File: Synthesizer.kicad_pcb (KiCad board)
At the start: 6 copper layers, 135.2 x 94.2 mm, 156 parts, among them J1 USB_A, J2 AudioJack3, J3 USB_B_Micro, J4 FPGA_debug, J5 MCU_debug, J6 MCU_GPIO, J7 FPGA_GPIO, SW1 SW_Push, SW10 SW_Push, SW11 SW_Push, SW12 SW_Push, SW13 SW_Push, SW14 SW_Push, SW15 SW_Push, SW16 SW_Push, SW2 SW_Push, SW3 SW_Push, SW4 SW_Push, SW5 SW_Push, SW6 SW_Push, SW7 SW_Push, SW8 SW_Push, SW9 SW_Push, U1 TPD3S014, U2 S25FL127S, U3 XC7A100T-FTG256, U4 Oscillator, U5 TPS54325, U6 TPS54294, U7 EFM32GG11B4xx, U8 PCM5102, Y1 48Mhz

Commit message: Fix one erroneous trace. VERY REVOLUTIONARY CHANGES
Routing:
- net +3V3: track 632.8 -> 632.2 mm
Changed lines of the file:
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@@
     (thickness 1.6)
     (drawings 4)
-    (tracks 1936)
+    (tracks 1935)
     (zones 0)
     (modules 156)
@@
   (segment (start 103.112 83.0343) (end 103.112 84.1636) (width 0.3) (layer F.Cu) (net 4))
   (segment (start 103.112 84.1636) (end 103.124 84.1756) (width 0.3) (layer F.Cu) (net 4))
-  (segment (start 107.3586 85.344) (end 108.0336 85.344) (width 0.3) (layer B.Cu) (net 4))
   (via (at 97.8662 87.9348) (size 0.48) (drill 0.25) (layers F.Cu B.Cu) (net 4))
   (segment (start 96.6995 87.9468) (end 97.8542 87.9468) (width 0.3) (layer F.Cu) (net 4))

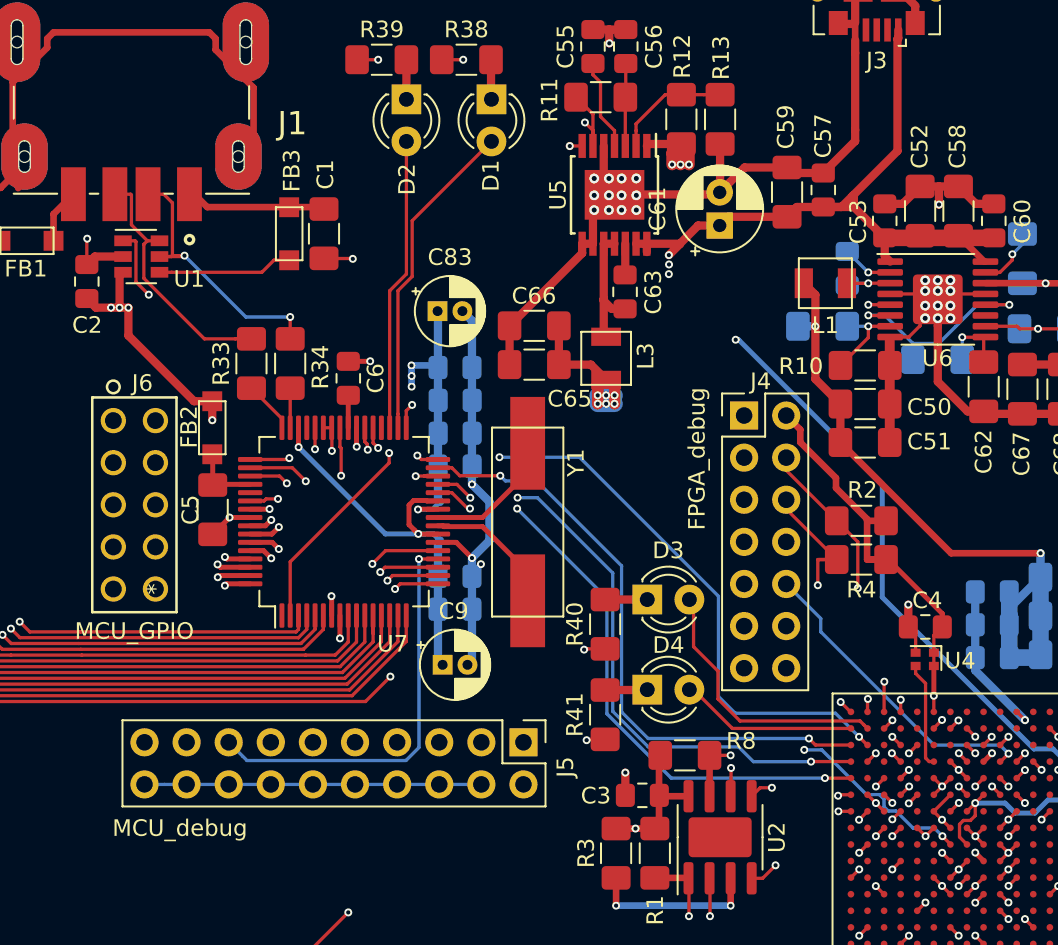
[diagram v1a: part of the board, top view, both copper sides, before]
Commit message: Changed a capacitor value from 100u to 150u. (oopsiedaisy)
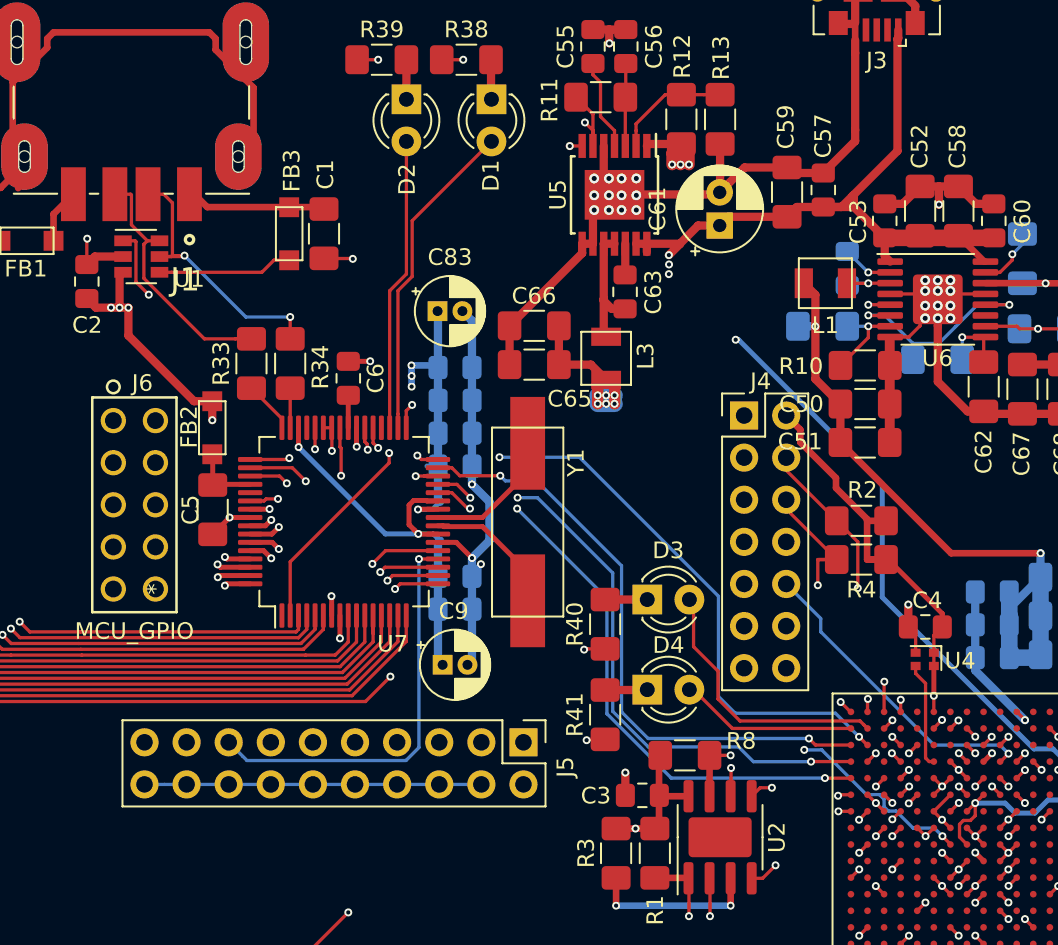
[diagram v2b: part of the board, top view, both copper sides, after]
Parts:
- removed the G*** at (171.3, 132.0)
- C1: value 100u -> 150u
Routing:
- net +3V3: track 632.2 -> 632.8 mm

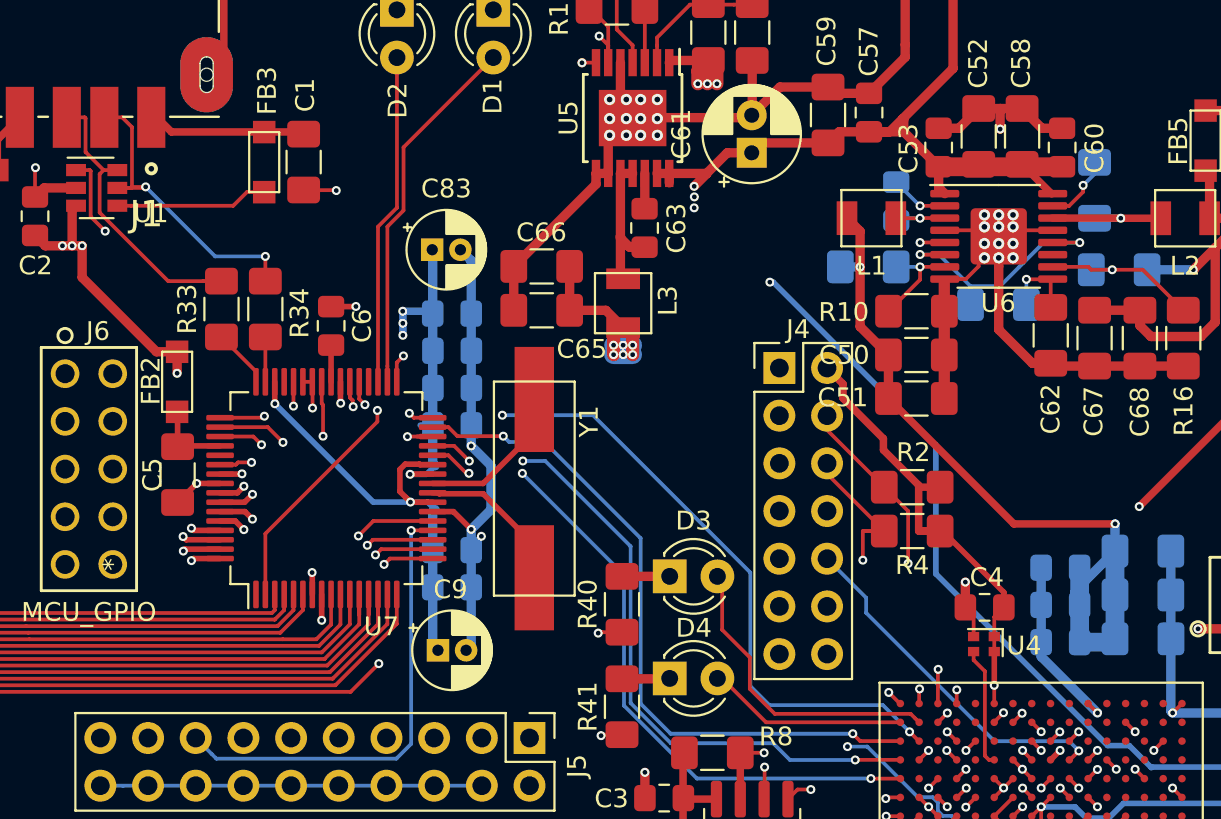
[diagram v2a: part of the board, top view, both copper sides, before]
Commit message: Replaced oscillator with a larger footprint and rewired. Also changed track width on some USB-A wires.
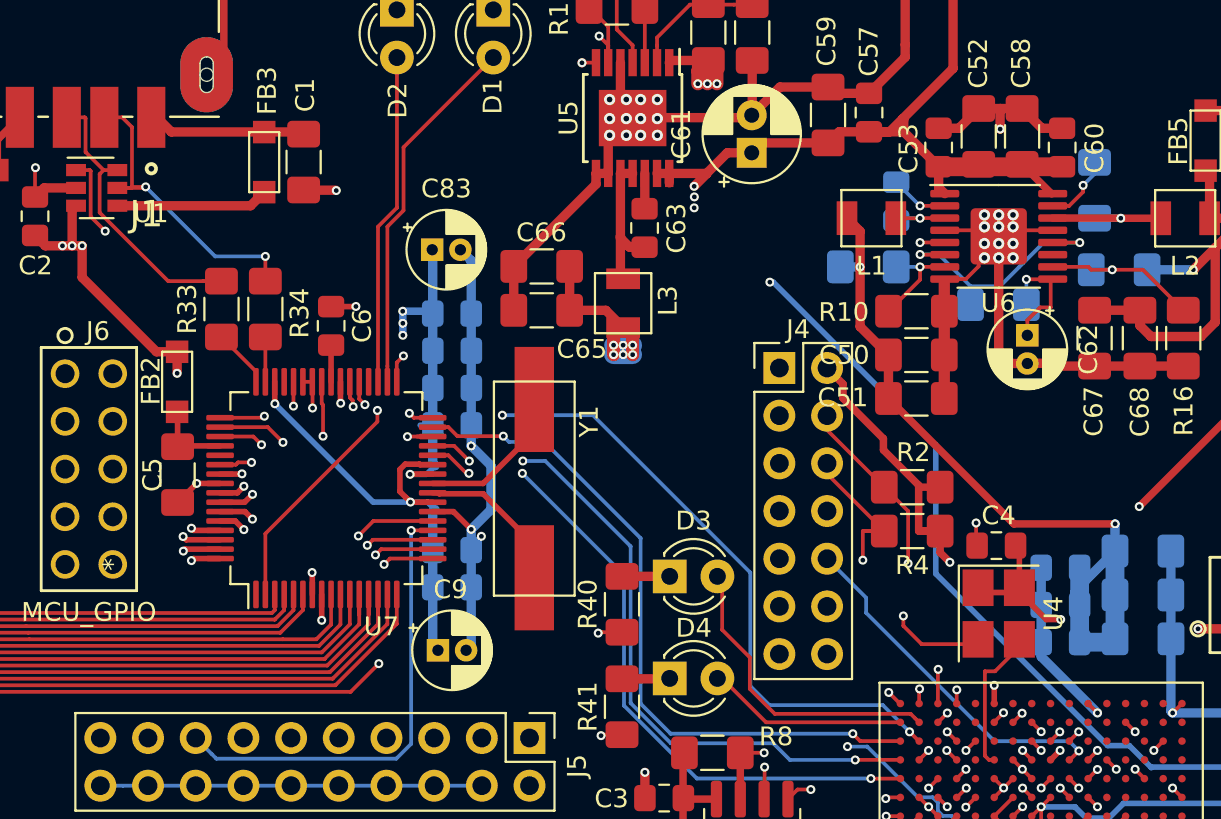
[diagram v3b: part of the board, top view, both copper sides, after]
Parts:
- C62: footprint Capacitor_SMD:C_1206_3216Metric_Pad1.42x1.75mm_HandSolder -> Capacitor_THT:CP_Radial_D4.0mm_P1.50mm
- U4: footprint Oscillator:Oscillator_SMD_Abracon_ASCO-4Pin_1.6x1.2mm -> Oscillator:Oscillator_SMD_Abracon_ASE-4Pin_3.2x2.5mm_HandSoldering
- moved C4 3.35 mm to (138.0, 91.8)
- moved U4 1.81 mm to (138.2, 95.4)
- moved C62 1.24 mm to (139.7, 80.6)
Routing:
- net GND: track 340.3 -> 344.0 mm, vias 96 -> 97
- net Net-(C62-Pad1): track 4.31 -> 6.64 mm
- net Net-(U3-PadN11): track 6.39 -> 7.61 mm
- net +3V3: track 632.8 -> 632.4 mm, vias 31 -> 33

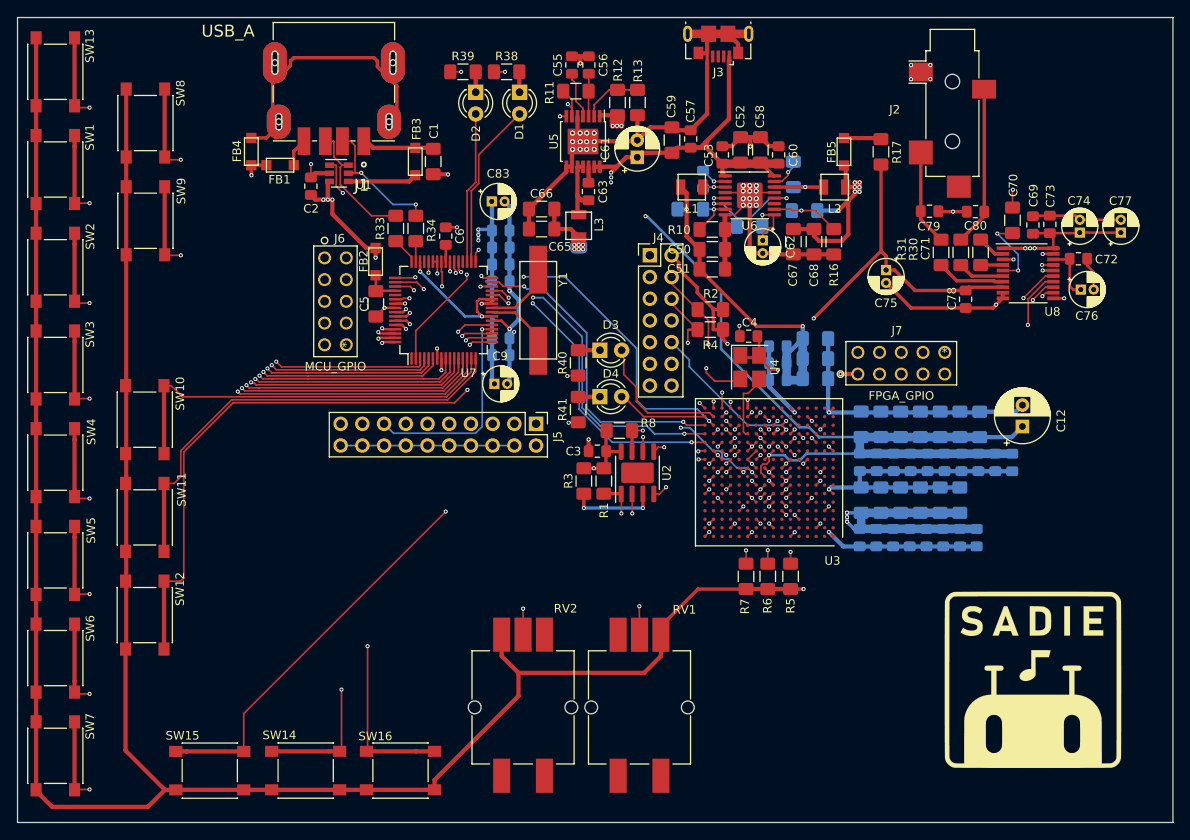
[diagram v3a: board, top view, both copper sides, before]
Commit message: Move FPGA decoupling caps. Rewire some PWR/GND pins
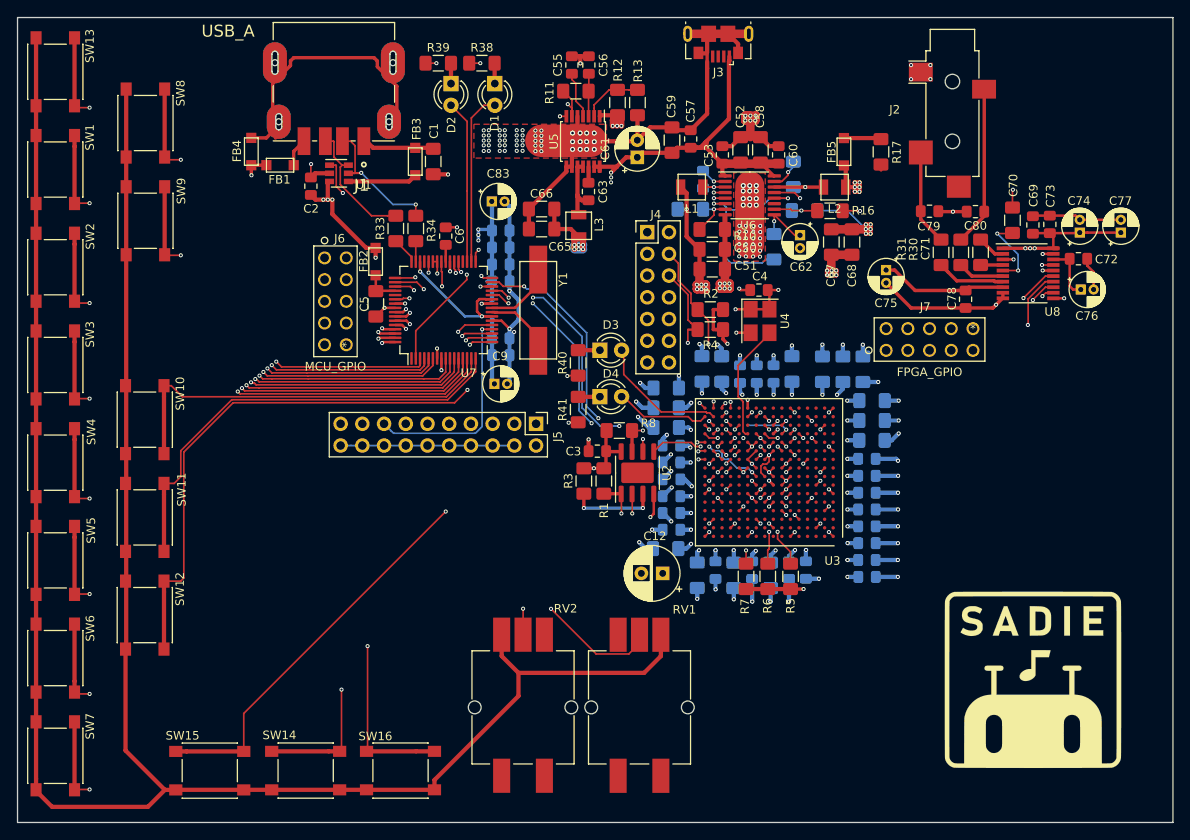
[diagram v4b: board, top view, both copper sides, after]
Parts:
- moved C12 45.4 mm to (128.0, 119.5), turned to 180 degrees
- moved C31 33.5 mm to (132.0, 119.7), turned to 270 degrees
- moved C38 33.2 mm to (134.2, 119.1)
- moved C28 33.2 mm to (128.3, 116.6), turned to 180 degrees
- moved C40 32.0 mm to (129.0, 104.6), turned to 180 degrees
- moved C33 31.8 mm to (136.3, 119.7), turned to 270 degrees
- moved C13 30.2 mm to (140.6, 119.7), turned to 270 degrees
- moved C22 30.0 mm to (129.0, 106.5), turned to 180 degrees
- moved C42 28.0 mm to (129.0, 108.5), turned to 180 degrees
- moved C46 27.5 mm to (138.5, 119.1)
- moved C25 27.4 mm to (128.4, 102.4), turned to 180 degrees
- moved C37 27.2 mm to (142.8, 119.1)
- moved C35 27.2 mm to (144.7, 119.1)
- moved C44 26.3 mm to (129.0, 110.5), turned to 180 degrees
- moved C21 25.2 mm to (128.4, 100.1), turned to 180 degrees
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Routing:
- net +3V3: track 632.4 -> 463.0 mm, vias 33 -> 49
- net +1V0: track 148.3 -> 50.3 mm, vias 15 -> 31
- net +3.3VA: track 103.0 -> 40.2 mm, vias 3 -> 2
- net +1V8: track 83.4 -> 31.7 mm, vias 5 -> 16
- net /Artix7/DAC_LRCK: track 72.5 -> 49.2 mm
- net Net-(R14-Pad2): track 13.9 -> 24.4 mm
- net GND: track 344.0 -> 335.7 mm, vias 97 -> 218
- net Net-(J4-Pad10): track 18.8 -> 26.8 mm
- net Net-(RV1-Pad2): track 58.6 -> 66.4 mm
- net Net-(J7-Pad5): track 25.2 -> 31.9 mm
- net Net-(U3-PadN11): track 7.61 -> 14.0 mm
- net Net-(J7-Pad8): track 21.8 -> 27.2 mm
- net Net-(J7-Pad4): track 19.1 -> 24.2 mm
- net Net-(J7-Pad6): track 18.0 -> 22.6 mm
- net Net-(J7-Pad2): track 14.9 -> 19.4 mm
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- added copper zone on F.Cu, net GND

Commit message: add power planes, spam vias everywhere
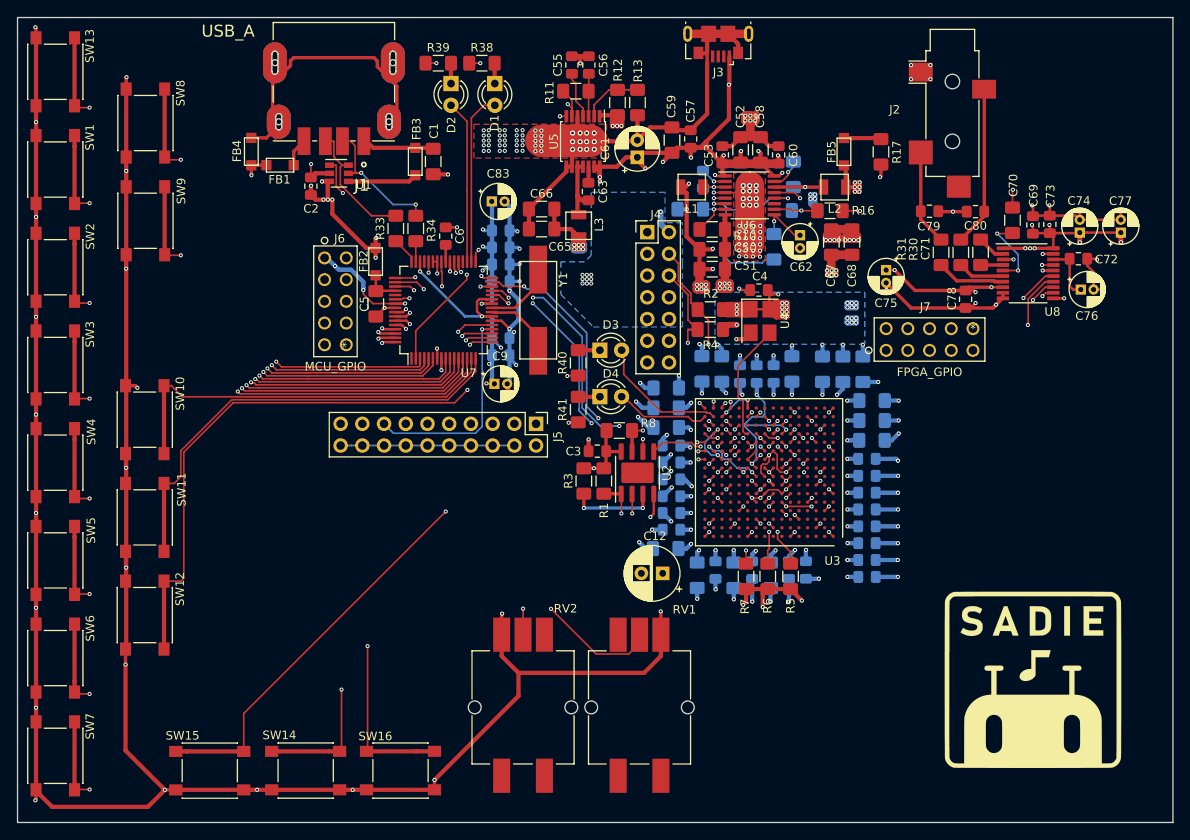
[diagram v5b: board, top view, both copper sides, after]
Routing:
- net +3V3: track 463.0 -> 504.9 mm, vias 49 -> 119
- net +5V: track 105.5 -> 75.0 mm, vias 8 -> 20
- net GND: track 335.7 -> 360.0 mm, vias 218 -> 232
- net +1V8: track 31.7 -> 50.6 mm, vias 16 -> 19
- net +1V0: track 50.3 -> 58.7 mm
- net +3.3VA: track 40.2 -> 46.6 mm, vias 2 -> 9
- added copper zone on PWR_plane, net +1V0
- added copper zone on PWR_plane, net +1V8
- added copper zone on PWR_plane, net +3.3VA
- added copper zone on B.Cu, net +3V3
- added copper zone on PWR_plane, net +3V3
- added copper zone on PWR_plane, net +5V

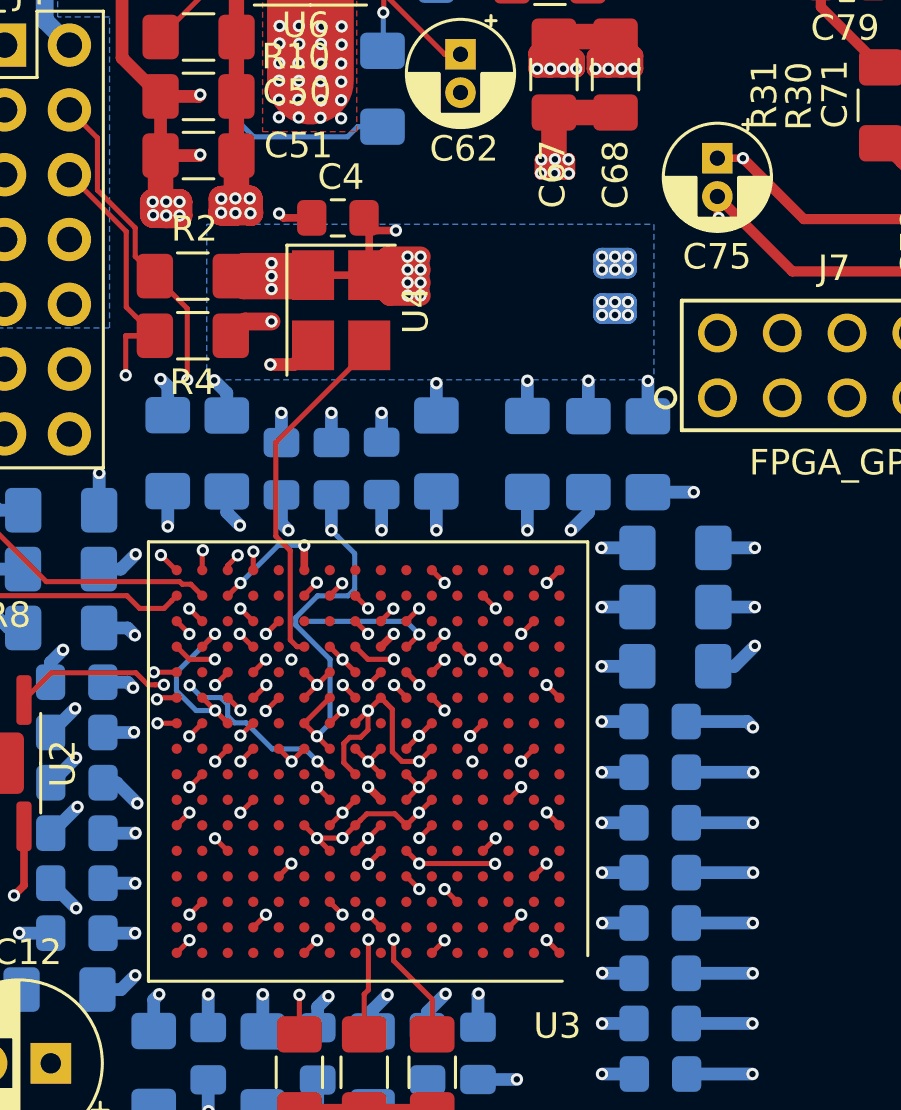
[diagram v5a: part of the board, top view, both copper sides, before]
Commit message: Thicken some power traces under the FPGA
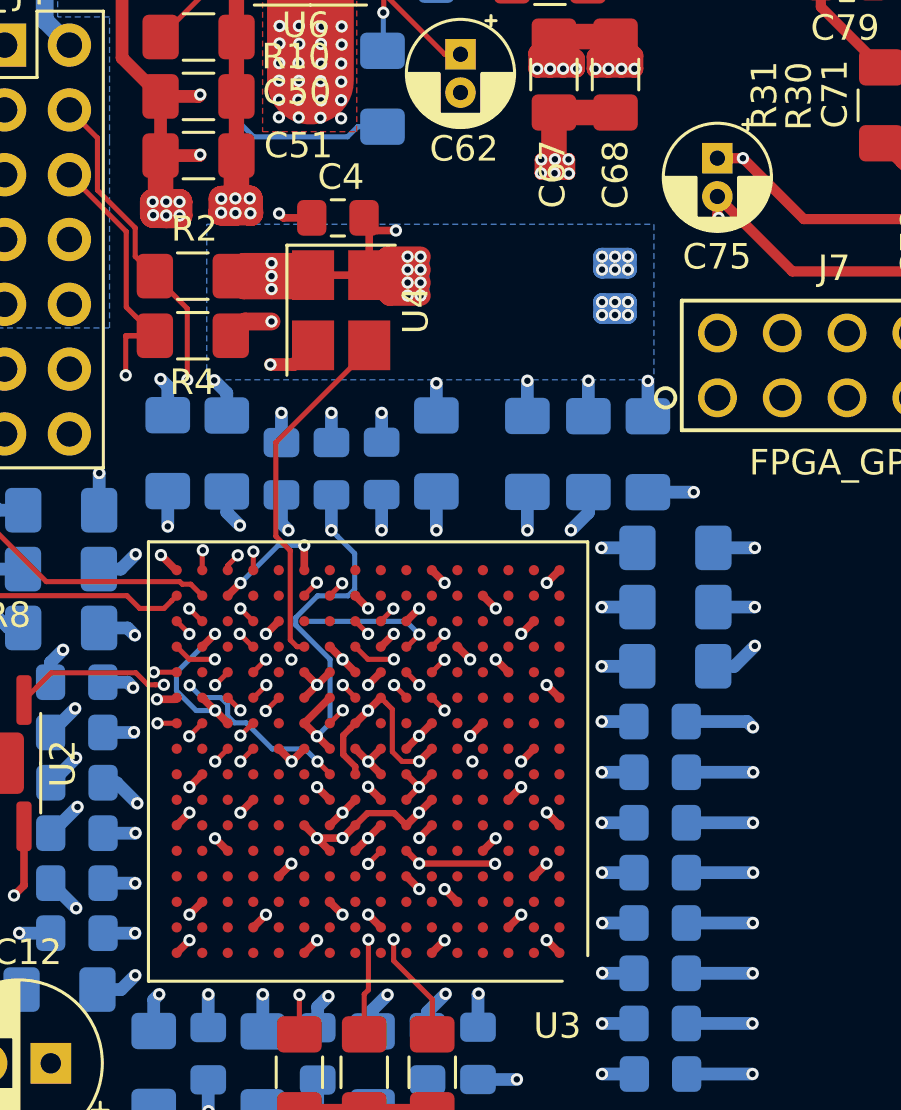
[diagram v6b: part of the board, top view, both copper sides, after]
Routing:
- net +3V3: track 504.9 -> 504.1 mm
- net +1V8: track 50.6 -> 51.3 mm
